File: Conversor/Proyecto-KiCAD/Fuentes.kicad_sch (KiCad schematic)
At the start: 0 parts

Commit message: Completar las fuentes aisladas del lado digital
- Falta hacer las fuentes del lado de potencia (sin las TRACO).
  - Se tiene que tomar la entrada de 12V-18V y pasarla por un regulador de 15V.
  - Despues esa salida de 15V se pasa por un regulador que la baje a 5V.
- Agregadas datasheets y notas:
  - Datasheets de regulador LM1117 para pasar de 5V a 3.3V para alimentar el DSP.
  - Notas de aplicacion de la fuente TRACO y explicaciones de corrientes sink y source.
- Hay que ver las cosas que me tiene que pasar Jorge de la alimentacion del DSP.
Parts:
- added C?: CREG_OUT, symbol Device:C_Small
- added C?: CFIN, symbol Device:C_Small
- added C?: CREG_IN, symbol Device:C_Small
- added J?: ConnAlim12-18, symbol Connector_Generic:Conn_01x02
- added U?: THB3-1211, symbol Componentes proyecto:THB3-1211
- added U?: LM1117-3.3, symbol Regulator_Linear:LM1117-3.3
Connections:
- new net: C?.1, J?.1 (Pin_1), U?.1 (+VIN)
- new net: C?.2, J?.2 (Pin_2), U?.23 (-VIN), U?.24 (-VIN)
- new net +3.3VD: C?.1, U?.2 (VO)
- new net +5VD: C?.1, U?.13 (+VOUT), U?.3 (VI)
- new net GNDD: C?.2, C?.2, U?.1 (GND), U?.12 (-VOUT)
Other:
- note added: "10uF"
- note added: "4.7uF"
- note added: "A DSP"
- note added: "Digital"
- note added: "Potencia"
- note added: "Valim+"
- note added: "Valim-"

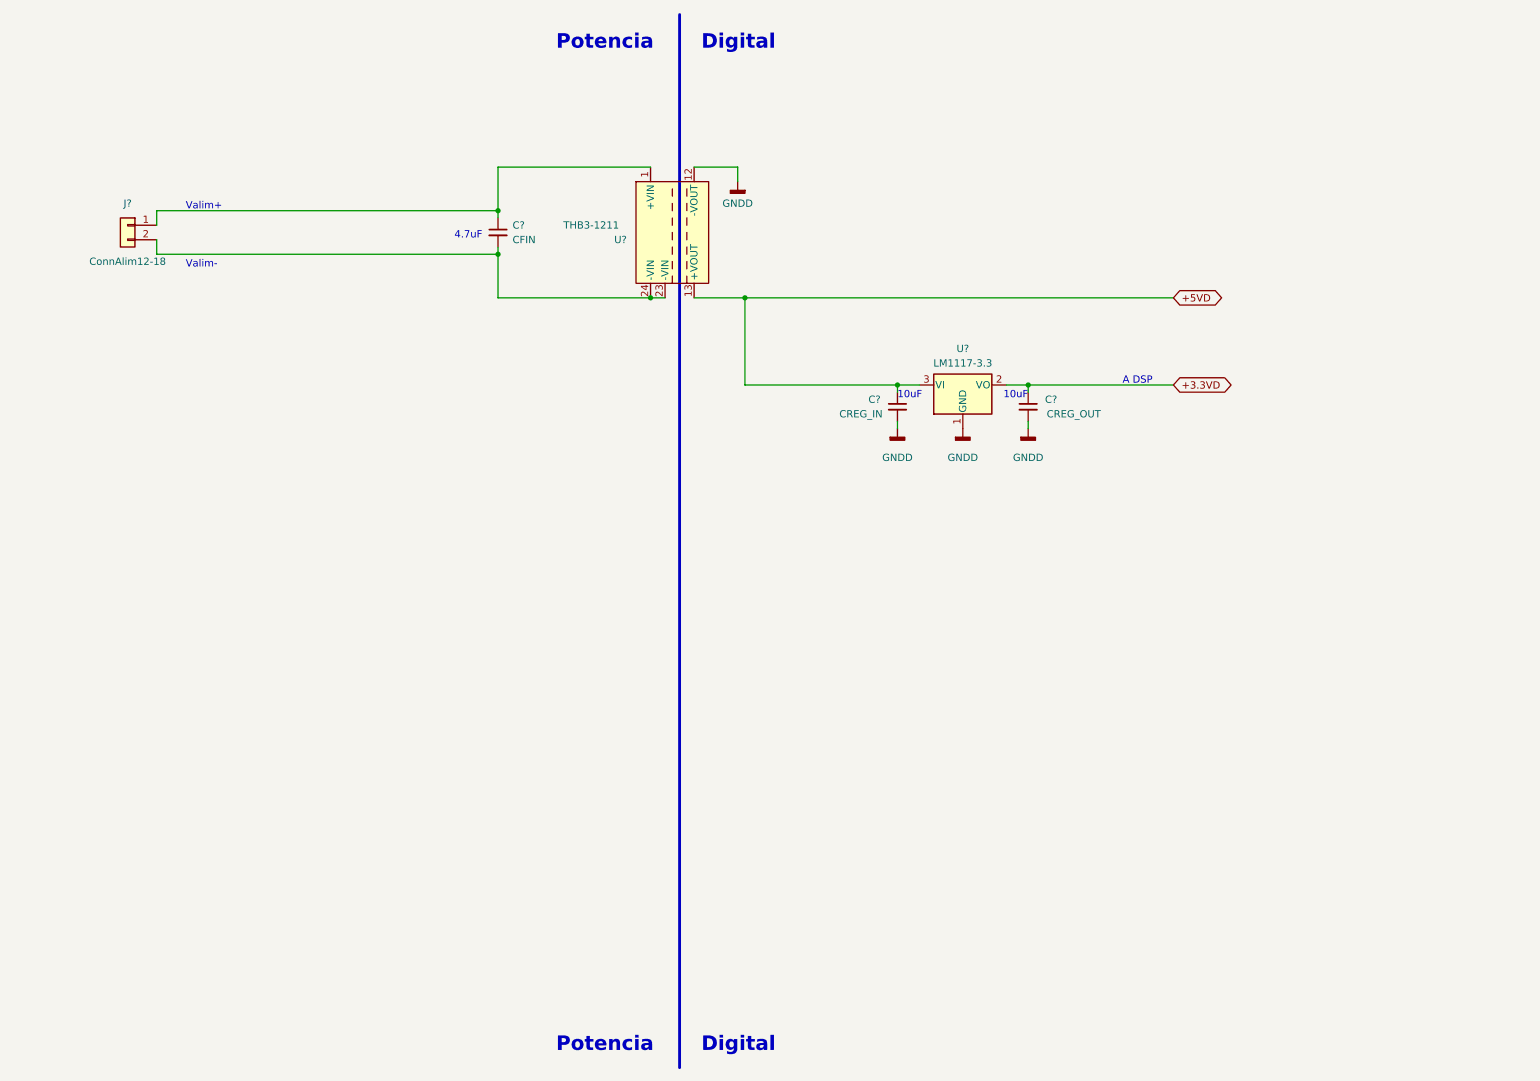
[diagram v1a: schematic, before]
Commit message: Seguir el trabajo en el esquematico de las fuentes
- Agregado un resumen de los consumos de corriente de todos los
integrados.
- Agregado un regulador para obtener +1.8VD, que al final no es
necesario porque la plaqueta del DSP se alimenta con 3.3 y 5
aparentemente (preguntar).
- Agregar el proyecto de Altium de la placa adaptadora para el DSP.
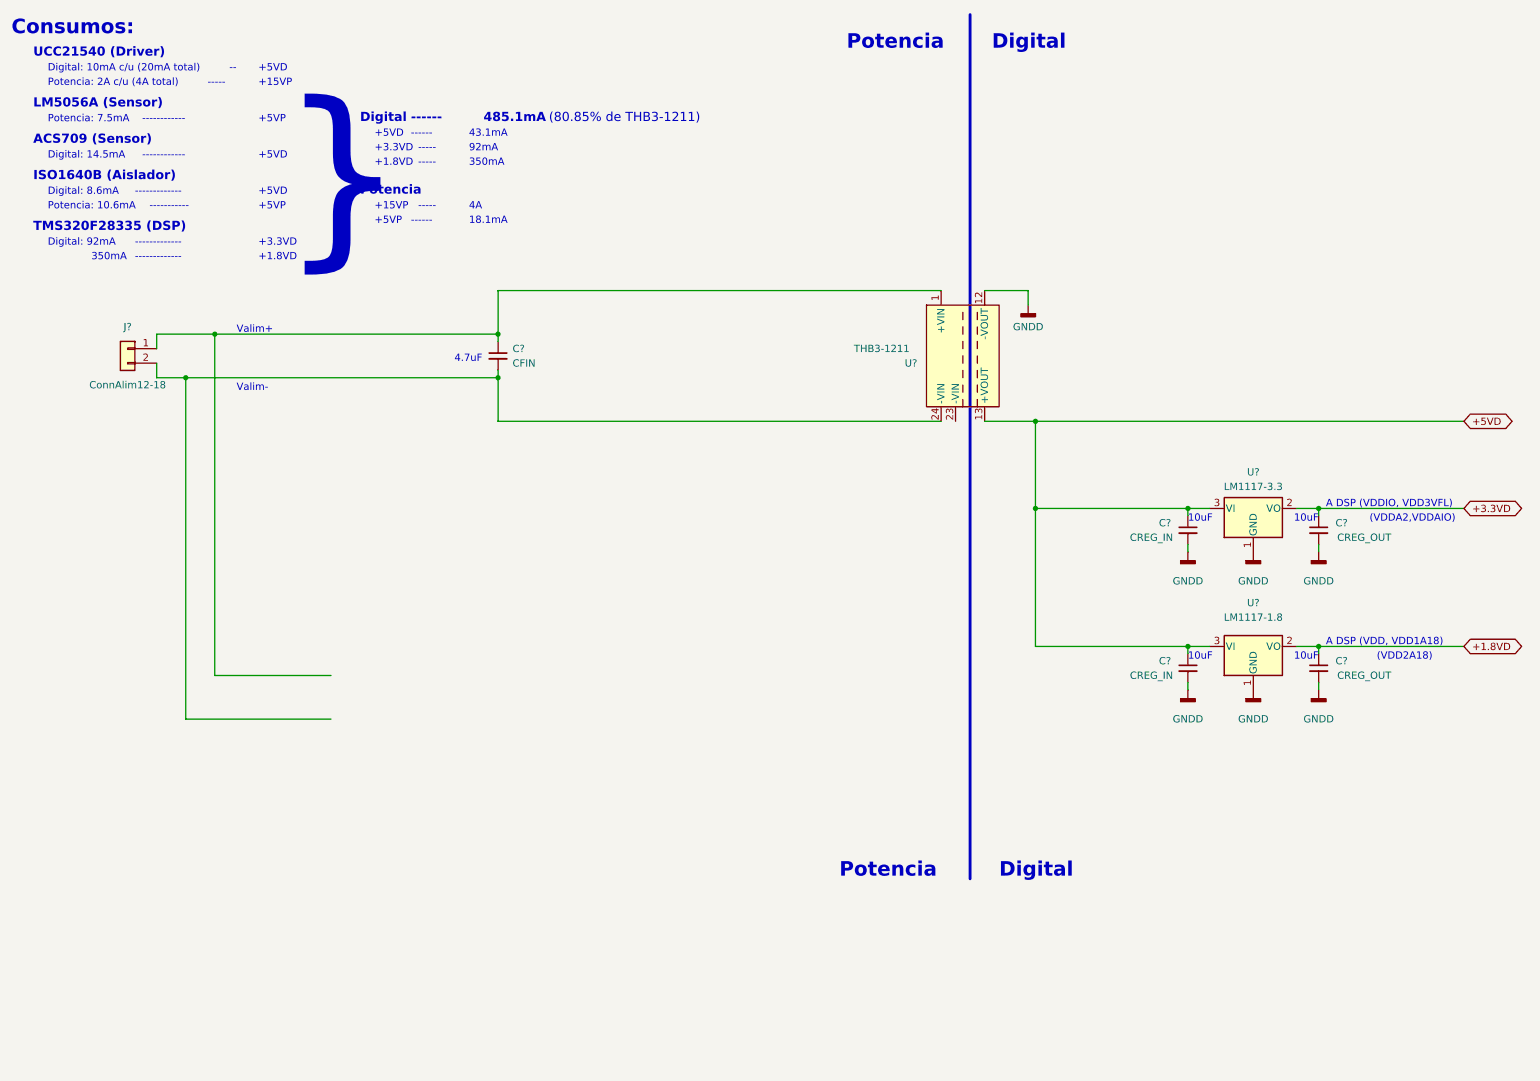
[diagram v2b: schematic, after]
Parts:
- added C?: CREG_OUT, symbol Device:C_Small
- added C?: CREG_IN, symbol Device:C_Small
- added U?: LM1117-1.8, symbol Regulator_Linear:LM1117-1.8
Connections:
- net +5VD: now also C?.1, U?.3 (VI)
- net GNDD: now also C?.2, C?.2, U?.1 (GND)
- net at C?.2, J?.2 (Pin_2), U?.24 (-VIN): no longer U?.23 (-VIN)
- new net +1.8VD: C?.1, U?.2 (VO)
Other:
- note added: "(80.85% de THB3-1211)"
- note added: "(VDD2A18)"
- note added: "(VDDA2,VDDAIO)"
- note added: "+1.8VD"
- note added: "+15VP"
- note added: "+3.3VD"
- note added: "+5VD"
- note added: "+5VP"
- note added: "--"
- note added: "-----"
- note added: "------"
- note added: "-----------"
- note added: "------------"
- note added: "-------------"
- note added: "18.1mA"
- note added: "350mA"
- note added: "43.1mA"
- note added: "485.1mA"
- note added: "4A"
- note added: "92mA"
- note added: "A DSP (VDD, VDD1A18)"
- note added: "A DSP (VDDIO, VDD3VFL)"
- note added: "ACS709 (Sensor)"
- note added: "Consumos:"
- note added: "Digital: 10mA c/u (20mA total)"
- note added: "Digital: 14.5mA"
- note added: "Digital: 8.6mA"
- note added: "Digital: 92mA"
- note added: "ISO1640B (Aislador)"
- note added: "LM5056A (Sensor)"
- note added: "Potencia: 10.6mA"
- note added: "Potencia: 2A c/u (4A total)"
- note added: "Potencia: 7.5mA"
- note added: "TMS320F28335 (DSP)"
- note added: "UCC21540 (Driver)"
- note added: "}"
- note removed: "A DSP"
- moved on the sheet: C?, J?, U?

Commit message: Modificar las fuentes de alimentacion
- Falta la fuente regulada de 15V para Vdd de los drivers (Sale a partir de alimentacion de 24V?)
- El DSP se alimenta por +5V a traves de la placa de prueba
- 3.3V para la proteccion a la salida del AO del ACS709
- Agregada datasheet del regulador MC7805 de 12-18V a 5VP
- Uso el pin de dead-time (DT) de los drivers para evitar corto en una pata del
  puente de MOSFETs (200ns de dead-time)
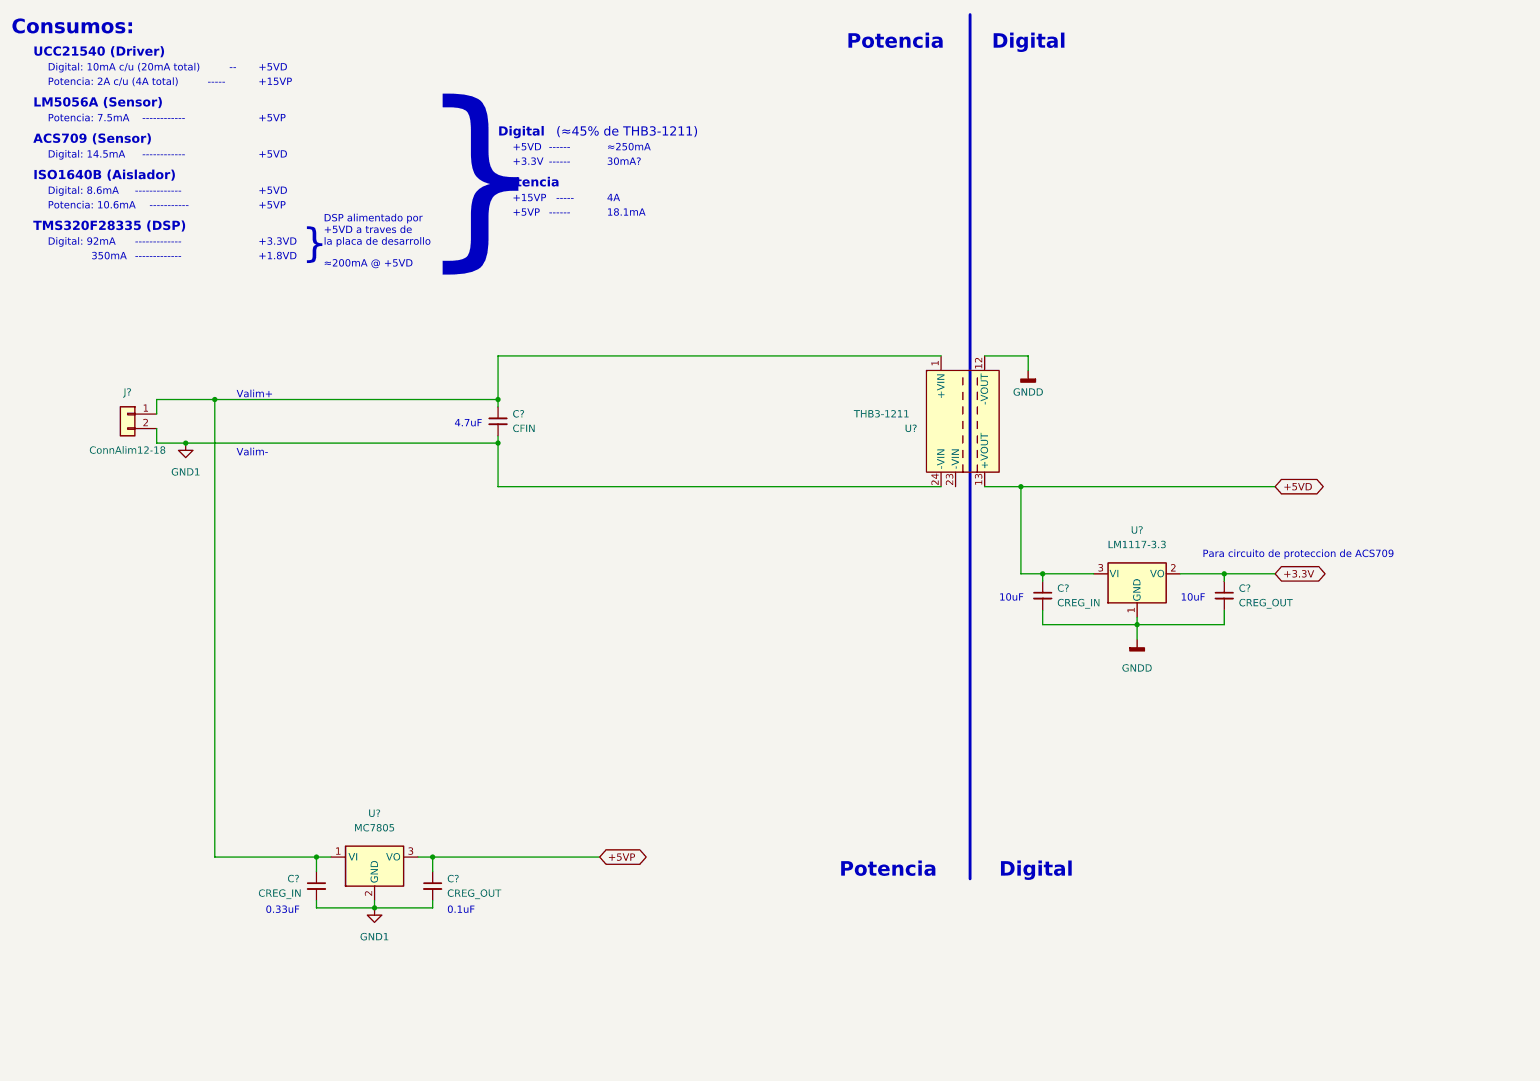
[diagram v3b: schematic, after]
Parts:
- removed C? (x2): CREG_OUT, symbol Device:C_Small
- removed C? (x2): CREG_IN, symbol Device:C_Small
- removed U?: LM1117-1.8, symbol Regulator_Linear:LM1117-1.8
- removed U?: LM1117-3.3, symbol Regulator_Linear:LM1117-3.3
- added C? (x2): CREG_OUT, symbol Device:C_Small
- added C? (x2): CREG_IN, symbol Device:C_Small
- added U?: MC7805, symbol Componentes proyecto:MC7805
- added U?: LM1117-3.3, symbol Regulator_Linear:LM1117-3.3
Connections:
- net +5VD: now also C?.1, U?.3 (VI)
- net GNDD: now also C?.2, C?.2, U?.1 (GND)
- net at C?.1, J?.1 (Pin_1), U?.1 (+VIN): now also C?.1, U?.1 (VI)
- net GND1: now reaches C?.2, J?.2 (Pin_2), U?.24 (-VIN)
- net GND1: now also C?.2, C?.2, U?.2 (GND)
- new net +3.3V: C?.1, U?.2 (VO)
- new net +5VP: C?.1, U?.3 (VO)
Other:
- note added: "(≈45% de THB3-1211)"
- note added: "+3.3V"
- note added: "0.1uF"
- note added: "0.33uF"
- note added: "30mA?"
- note added: "DSP alimentado por +5VD a traves de la placa de desarrollo"
- note added: "Para circuito de proteccion de ACS709"
- note added: "≈200mA @ +5VD"
- note added: "≈250mA"
- note removed: "(80.85% de THB3-1211)"
- note removed: "(VDD2A18)"
- note removed: "(VDDA2,VDDAIO)"
- note removed: "43.1mA"
- note removed: "485.1mA"
- note removed: "92mA"
- note removed: "A DSP (VDD, VDD1A18)"
- note removed: "A DSP (VDDIO, VDD3VFL)"
- moved on the sheet: C?, J?, U?

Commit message: Cambiar	drivers	por ADuM4221 de	Analog y completar alimentacion
- UCC21540 y UCC27200 sin stock:
	- Reemplazado por el ADuM4221/ADuM4221-1 de Analog, que es muy similar
	- Alternativa el LTC7061, que tiene DT pero no es aislado
- Aisladores sin stock, falta buscar un reemplazo
- Agregadas las hojas de datos
- LM5056A con poco stock (Hay que comprar muy pronto)
- Completada la lista de componentes con todos los integrados/diodos/transistores
- Agregada nota de aplicacion sobre peak source y sink current
- Agregadas bibliotecas del ADuM4421 y LM5056A bajadas de las paginas de Analog y TI respectivamente
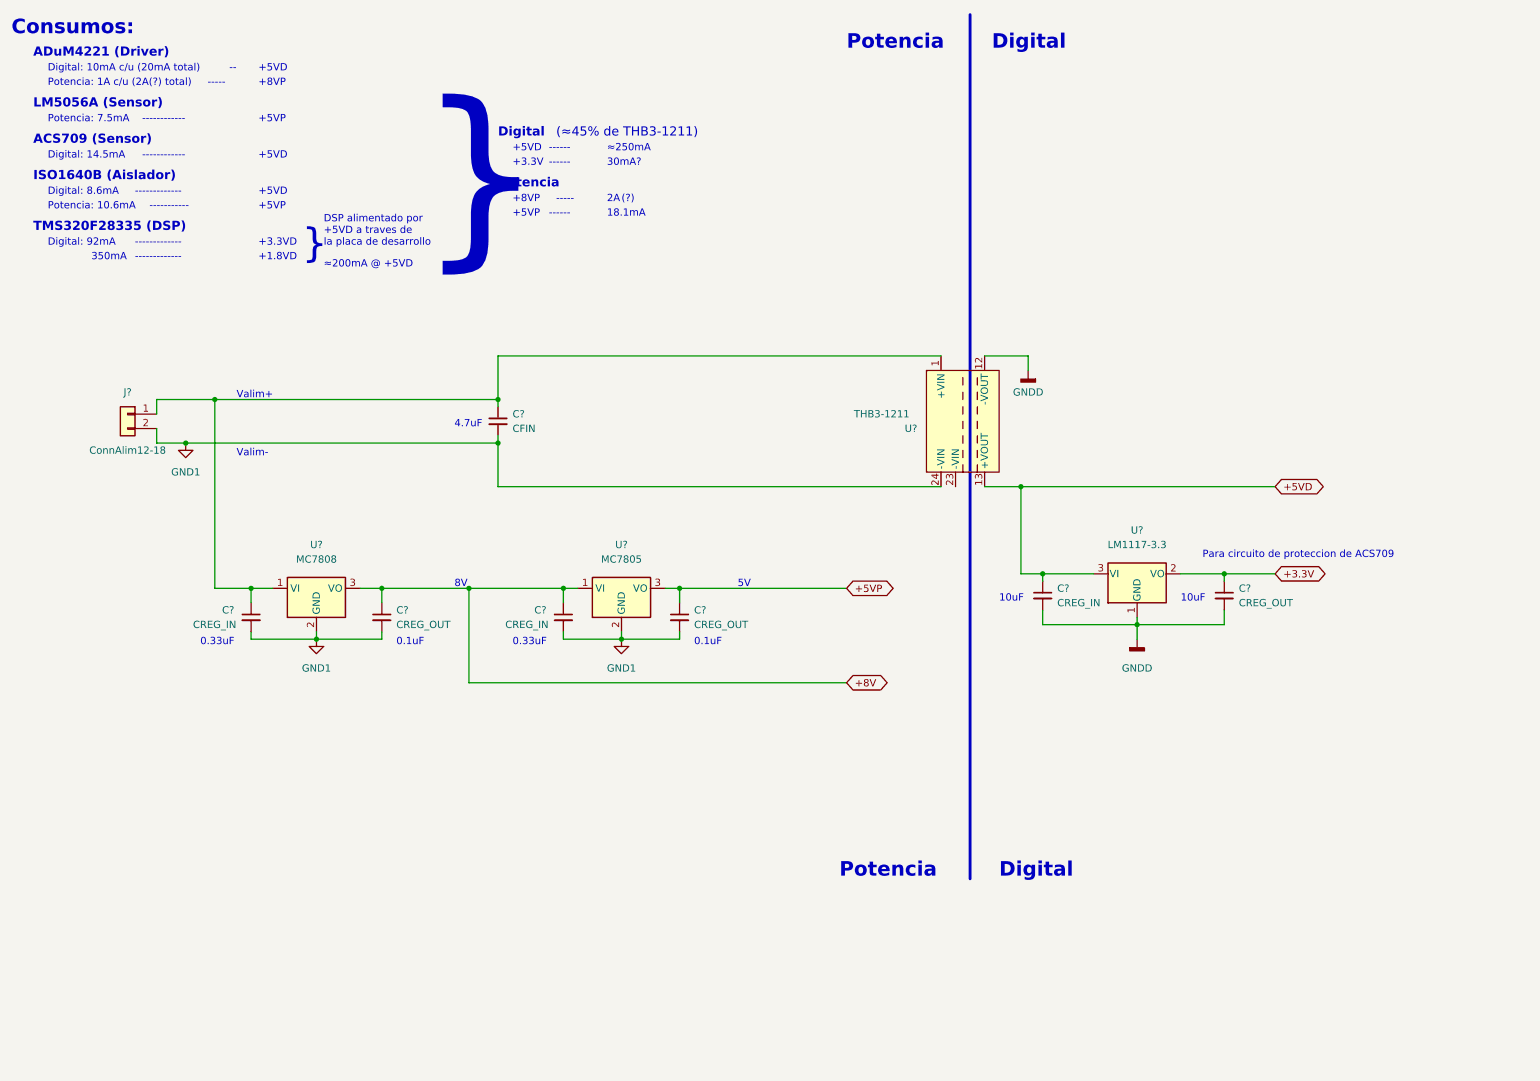
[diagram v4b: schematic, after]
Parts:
- added C?: CREG_OUT, symbol Device:C_Small
- added C?: CREG_IN, symbol Device:C_Small
- added U?: MC7808, symbol Componentes proyecto:MC7808
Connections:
- net GND1: now also C?.2, C?.2, U?.2 (GND)
- net at C?.1, J?.1 (Pin_1), U?.1 (+VIN): now also C?.1, U?.1 (VI); no longer C?.1, U?.1 (VI)
- new net +8V: C?.1, C?.1, U?.1 (VI), U?.3 (VO)
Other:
- note added: "(?)"
- note added: "+8VP"
- note added: "2A"
- note added: "5V"
- note added: "8V"
- note added: "ADuM4221 (Driver)"
- note added: "Potencia: 1A c/u (2A(?) total)"
- note removed: "+15VP"
- note removed: "4A"
- note removed: "Potencia: 2A c/u (4A total)"
- note removed: "UCC21540 (Driver)"
- moved on the sheet: C?, U?
